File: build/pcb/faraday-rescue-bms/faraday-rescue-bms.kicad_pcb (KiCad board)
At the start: 4 copper layers, 481.3 x 23.7 mm, 155 parts, among them J1 532610571, J3 532610471, Q1 FCX495TA, Q3 2N7002, U1 BQ7697202, U2 STM32L010K8Tx, U4 THVD2410DR, Y1 ABS07-32.768KHZ-T

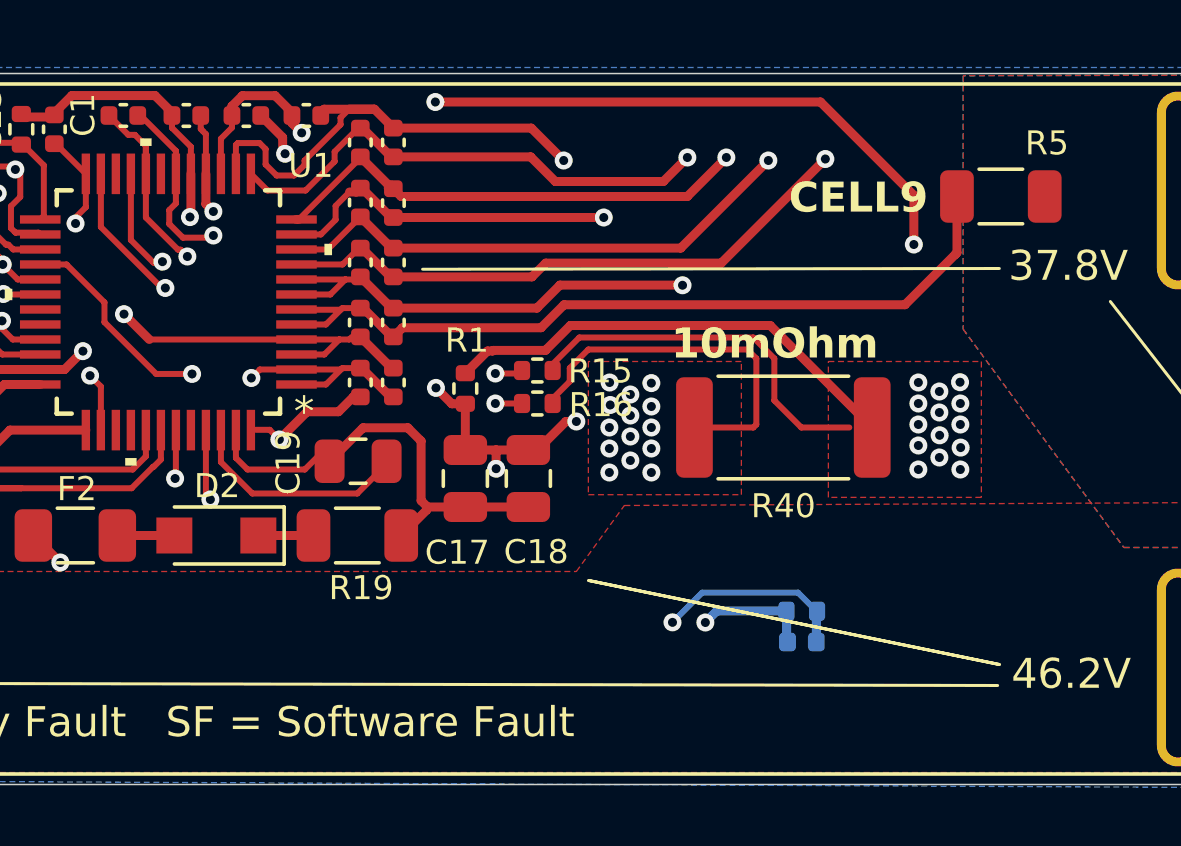
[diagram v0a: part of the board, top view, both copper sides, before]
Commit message: Fixed issue with latest version of gerber
A user had an issue related to an area fill. Pin 7 on the programming connector was intended to be connected to a power net, but became isolated after a zone fill. Also, VSS on the 1.8V LDO on the BQ chip was not connected.

If your board buzzes (put your ear close to the BQ chip) when you solder up all the batteries, this may be your issue. The rework is to short VSS on C14 to VSS on C16 and to add a wire between Net-(BT1-+-Pad3) and the big area fill to the left.
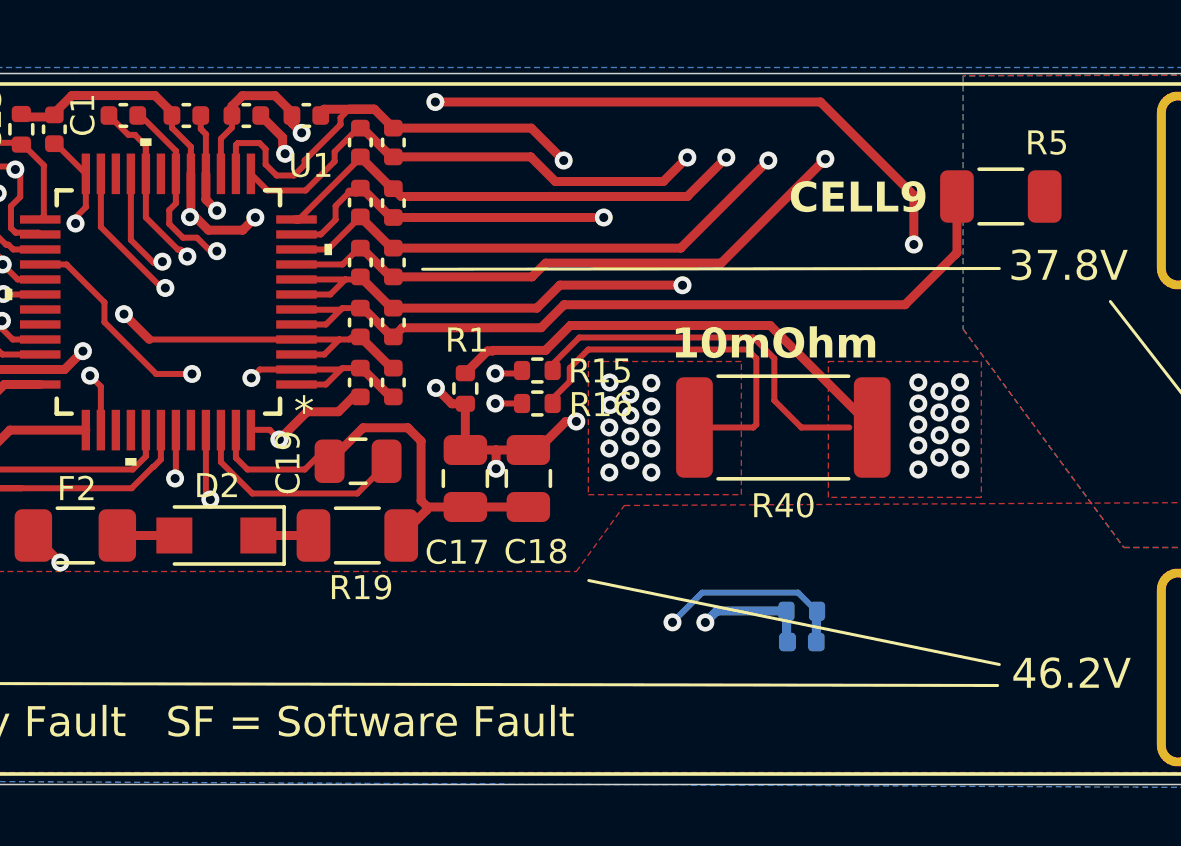
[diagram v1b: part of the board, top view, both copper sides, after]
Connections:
- J1 pad 7: (no net) -> Net-(BT1-+-Pad3)
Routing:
- net VSS: track 514.2 -> 516.8 mm, vias 32 -> 33
